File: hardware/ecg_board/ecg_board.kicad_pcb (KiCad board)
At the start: 2 copper layers, 53 parts, among them J1 USB_C_Receptacle_USB2.0_16P, J3 MEM2075-00-140-01-A, Q1 PMOS, U1 ESP32-S3-WROOM-1, U2 TLV75801PDBV, U3 AD8232, U4 MCP73832-2-OT, U5 USBLC6-2P6

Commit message: updated schematic and finish pcb v1
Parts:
- added BT1: Battery_Cell, Battery:battery_pads, F.Cu at (107.2, 69.4)
- added SW1: SW_SPDT, Button_Switch_SMD:SW_SPDT_PCM12, F.Cu at (109.4, 60.7)
- C10, C12, C13, C14: footprint Capacitor_SMD:C_0603_1608Metric -> Capacitor_SMD:C_0805_2012Metric
- E1, E2, E3: moved to B.Cu
- moved U3 132.8 mm to (179.5, 70.3), turned to 90 degrees
- moved E1 114.9 mm to (157.3, 97.1), turned to 180 degrees
- moved U2 94.0 mm to (134.7, 79.0)
- moved J3 93.5 mm to (197.6, 96.4), turned to 90 degrees
- moved U1 89.7 mm to (138.2, 101.5), turned to 180 degrees
- moved U5 89.4 mm to (149.9, 74.5), turned to 180 degrees
- moved U4 89.0 mm to (129.9, 65.0), turned to -90 degrees
- moved C9 82.2 mm to (148.9, 106.2), turned to -90 degrees
- moved C4 81.4 mm to (186.7, 68.8), turned to -90 degrees
- moved D1 81.4 mm to (133.1, 74.9), turned to -90 degrees
- moved C10 80.8 mm to (150.7, 106.4), turned to -90 degrees
- moved C5 78.9 mm to (183.7, 72.2), turned to 90 degrees
- moved C1 78.5 mm to (176.4, 74.8), turned to 180 degrees
- moved C6 76.9 mm to (181.4, 74.8)
- moved R13 76.8 mm to (189.7, 72.2), turned to -90 degrees
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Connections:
- net +BATT renamed Net-(Q1-D)
- net /RL renamed /LL
- C12 pad 2: +5V -> VDD
- J1 pad A6: unconnected-(J1-D+-PadA6) -> Net-(J1-D+-PadA6)
- J1 pad B5: Net-(J1-CC1) -> Net-(J1-CC2)
- J1 pad B6: unconnected-(J1-D+-PadB6) -> Net-(J1-D+-PadA6)
- J1 pad B7: unconnected-(J1-D--PadB7) -> Net-(J1-D--PadA7)
- R1 pad 1: unconnected-(R1-Pad1) -> Net-(J1-CC2)
- R2 pad 1: unconnected-(R2-Pad1) -> Net-(J1-CC1)
- U1 pad 26: /CS_SD -> unconnected-(U1-IO45-Pad26)
- U1 pad 33: /SCK -> unconnected-(U1-IO40-Pad33)
- U1 pad 34: /MISO -> unconnected-(U1-IO41-Pad34)
- U1 pad 35: /MOSI -> unconnected-(U1-IO42-Pad35)
- U1 pad 6: unconnected-(U1-IO6-Pad6) -> /MISO
- U1 pad 7: unconnected-(U1-IO7-Pad7) -> /SCK
- U1 pad 8: unconnected-(U1-IO15-Pad8) -> /MOSI
- U1 pad 9: unconnected-(U1-IO16-Pad9) -> /CS_SD
- U2 pad 1: +5V -> VDD
- U2 pad 3: +5V -> VDD
- U5 pad 3: Net-(J1-CC1) -> Net-(J1-D--PadA7)
- U5 pad 4: Net-(J1-D--PadA7) -> Net-(J1-D+-PadA6)
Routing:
- net +3V3: track 0.00 -> 93.8 mm, vias 0 -> 4
- net /RA: track 0.00 -> 84.7 mm, vias 0 -> 1
- net /SIG_OUT: track 0.00 -> 78.6 mm, vias 0 -> 2
- net /LO+: track 0.00 -> 54.2 mm, vias 0 -> 2
- net /LO-: track 0.00 -> 52.4 mm, vias 0 -> 2
- net +5V: track 0.00 -> 49.9 mm, vias 0 -> 3
- net Net-(Q1-D): track 0.00 -> 44.9 mm, vias 0 -> 2
- net /MOSI: track 0.00 -> 39.5 mm
- net /CS_SD: track 0.00 -> 39.5 mm
- net /SCK: track 0.00 -> 39.1 mm
- net /MISO: track 0.00 -> 38.8 mm
- net Net-(U3-SW): track 0.00 -> 28.7 mm, vias 0 -> 2
- net Net-(U3-IAOUT): track 0.00 -> 28.5 mm, vias 0 -> 2
- net /REFOUT: track 0.00 -> 28.3 mm, vias 0 -> 2
- net Net-(R17-Pad2): track 0.00 -> 21.8 mm, vias 0 -> 2
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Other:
- board outline added: 112 x 55.9 mm
- copper layers 2 -> 4
- board text added: "BATTERY"
- board text added: "FINGER ECG"

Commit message: added components and created bom
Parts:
- added C16: 220nF, Capacitor_SMD:C_0603_1608Metric, F.Cu at (176.4, 76.5)
- added C17: 220nF, Capacitor_SMD:C_0603_1608Metric, F.Cu at (165.8, 66.8)
- added R23: 470k, Resistor_SMD:R_0603_1608Metric, F.Cu at (168.3, 69.3)
- added R25: 220k, Resistor_SMD:R_0603_1608Metric, F.Cu at (183.8, 80.9)
- C1, C7: value 0.33uF -> 100nF
- C14: footprint Capacitor_SMD:C_0805_2012Metric -> Capacitor_SMD:C_0603_1608Metric
- C4: value 1.5nF -> 1nF
- D3: moved to B.Cu
- J1: footprint Connector_USB:USB_C_Receptacle_GCT_USB4105-xx-A_16P_TopMnt_Horizontal -> Connector_USB:USB_C_Receptacle_HCTL_HC-TYPE-C-16P-01A
- Q1: value PMOS -> NX3008PBK,215
- R14: value 360k -> 220k
- R15, R16: value 180k -> 220k
- R5: value 1.4M -> 1M
- moved C11 1.73 mm to (150.2, 102.3)
- moved R19 1.68 mm to (166.0, 70.2)
- moved R22 1.55 mm to (150.2, 103.9)
- moved D3 1.28 mm to (137.5, 67.2), turned to 180 degrees
- moved R1 0.98 mm to (147.5, 71.9)
- moved R2 0.90 mm to (152.1, 71.8)
- moved R15 0.75 mm to (179.8, 79.1)
- moved R16 0.75 mm to (177.7, 79.1)
- moved R17 0.75 mm to (175.7, 79.1)
- moved R18 0.75 mm to (181.7, 79.1)
- moved R14 0.58 mm to (183.8, 77.8)
- moved C7 0.20 mm to (167.5, 66.8)
- moved SW1 0.16 mm to (109.4, 60.8)
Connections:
- R14 pad 1: /LL -> Net-(R14-Pad1)
- R5 pad 2: Net-(U3-SW) -> Net-(R23-Pad1)
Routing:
- net +3V3: track 93.8 -> 167.3 mm, vias 4 -> 5
- net GND: track 0.00 -> 17.8 mm, vias 0 -> 45
- net /LA: track 17.7 -> 28.6 mm
- net /LL: track 7.26 -> 15.5 mm
- net Net-(R17-Pad2): track 21.8 -> 27.5 mm
- net /D-: track 14.0 -> 19.5 mm
- net /D+: track 14.3 -> 18.6 mm
- net Net-(J1-D--PadA7): track 7.68 -> 10.8 mm
- net Net-(J1-D+-PadA6): track 7.68 -> 10.6 mm
- net /REFOUT: track 28.3 -> 30.7 mm
- net VDD: track 10.9 -> 13.3 mm
- net Net-(D3-A): track 1.67 -> 3.46 mm, vias 0 -> 1
- net Net-(C4-Pad2): track 3.00 -> 4.73 mm
- net Net-(U3-HPSENSE): track 6.19 -> 7.86 mm
- net Net-(U3-HPDRIVE): track 3.21 -> 4.88 mm
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- added copper zone on B.Cu, net GND
- added copper zone on F.Cu, net GND
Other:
- outline, holes or cut-outs redrawn
- copper layers 4 -> 2
- board text removed: "FINGER ECG"

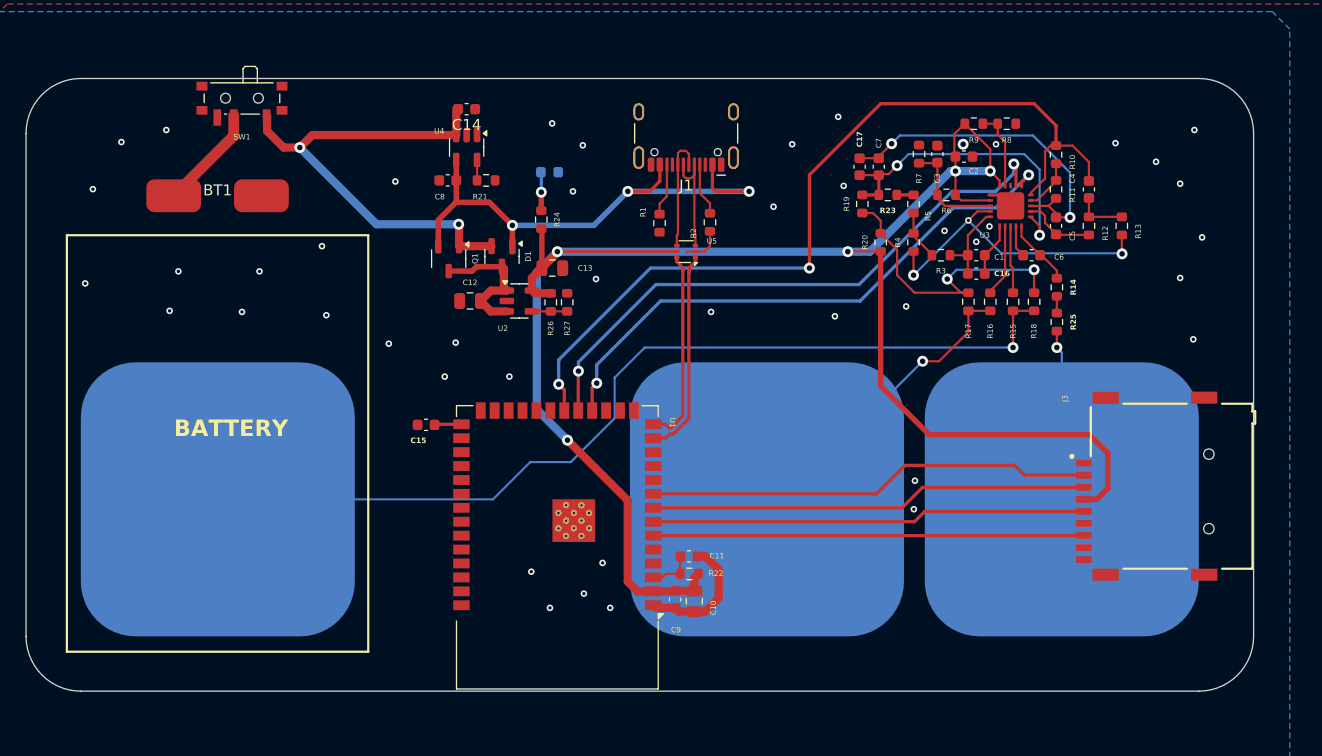
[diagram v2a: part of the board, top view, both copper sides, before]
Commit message: moved switch and fixed bom
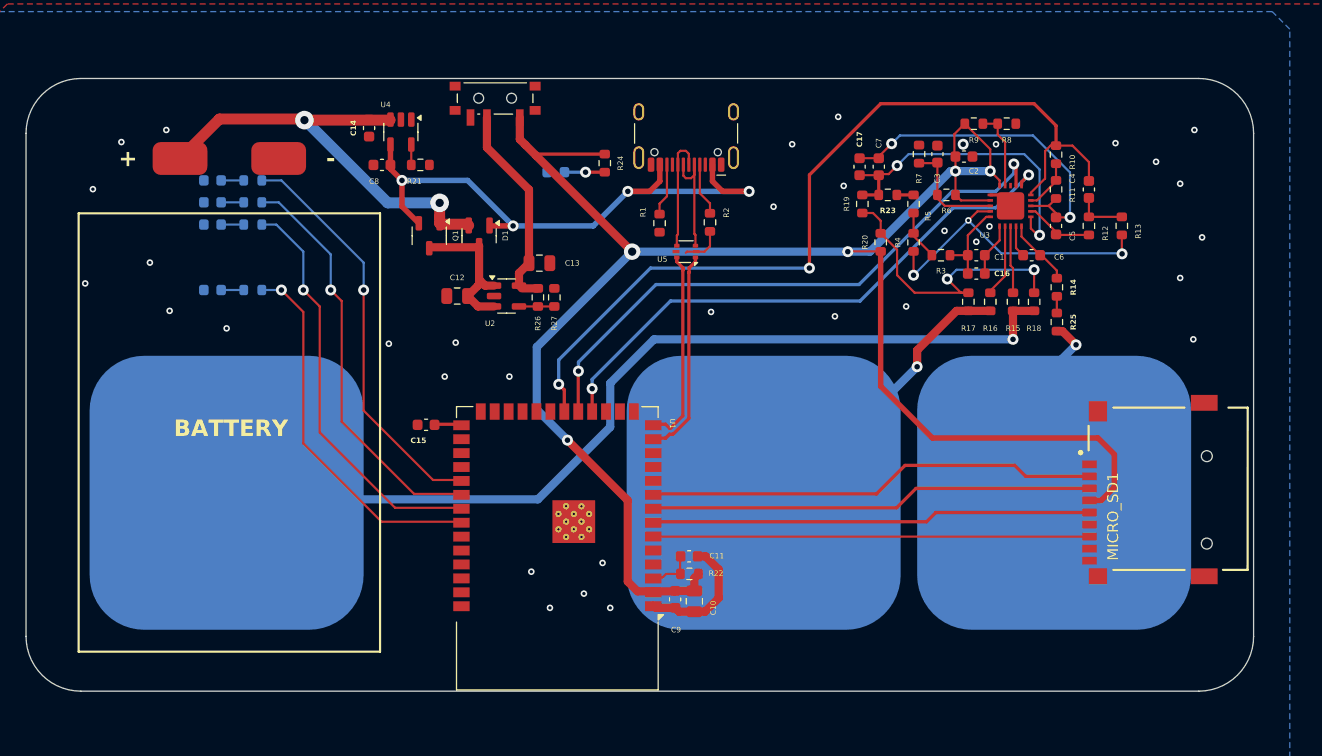
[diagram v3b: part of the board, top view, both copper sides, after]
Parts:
- removed J3: MEM2075-00-140-01-A, MEM2075_00_140_01_A:GCT_MEM2075-00-140-01-A
- added D2: LED, LED_SMD:LED_0603_1608Metric, B.Cu at (106.7, 72.0)
- added D4: LED, LED_SMD:LED_0603_1608Metric, B.Cu at (106.7, 70.0)
- added D5: LED, LED_SMD:LED_0603_1608Metric, B.Cu at (106.7, 68.0)
- added D6: LED, LED_SMD:LED_0603_1608Metric, B.Cu at (106.7, 78.0)
- added MICRO_SD1: TF-01A, TF-01A:TF-01A, F.Cu at (193.9, 96.1)
- added R28: 2k, Resistor_SMD:R_0603_1608Metric, B.Cu at (110.4, 72.0)
- added R29: 2k, Resistor_SMD:R_0603_1608Metric, B.Cu at (110.4, 70.0)
- added R30: 2k, Resistor_SMD:R_0603_1608Metric, B.Cu at (110.4, 68.0)
- added R31: 2k, Resistor_SMD:R_0603_1608Metric, B.Cu at (110.4, 78.0)
- moved SW1 23.1 mm to (132.5, 60.8)
- moved C14 9.07 mm to (121.0, 63.2), turned to 90 degrees
- moved R24 7.75 mm to (142.5, 66.4)
- moved C8 6.16 mm to (122.2, 66.6)
- moved R21 6.16 mm to (125.7, 66.6)
- moved U4 6.16 mm to (123.9, 63.6)
- moved BT1 3.57 mm to (108.2, 66.0)
- moved D1 2.81 mm to (131.0, 73.0)
- moved Q1 2.74 mm to (126.5, 73.0)
- moved C12 1.26 mm to (129.0, 78.5)
- moved C13 1.26 mm to (136.5, 75.5)
- moved U2 1.26 mm to (133.5, 78.5)
- moved R26 1.26 mm to (136.4, 78.7)
- moved R27 1.26 mm to (137.9, 78.7)
- moved E2 1.00 mm to (108.0, 96.5)
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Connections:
- C13 pad 2: +3V3 -> Net-(SW1-B)
- C14 pad 2: Net-(Q1-D) -> +BATT
- D1 pad 2: Net-(Q1-D) -> +BATT
- Q1 pad 1: Net-(Q1-D) -> +BATT
- R24 pad 1: Net-(D3-A) -> +3V3
- R24 pad 2: +3V3 -> Net-(D3-A)
- R26 pad 1: +3V3 -> Net-(SW1-B)
- SW1 pad 1: Net-(Q1-D) -> +3V3
- SW1 pad 2: +BATT -> Net-(SW1-B)
- U1 pad 31: unconnected-(U1-IO38-Pad31) -> /RECORDING
- U1 pad 32: unconnected-(U1-IO39-Pad32) -> /LEADS_ON
- U1 pad 33: unconnected-(U1-IO40-Pad33) -> /LEADS_OFF
- U1 pad 34: unconnected-(U1-IO41-Pad34) -> /EXTRA
- U2 pad 5: +3V3 -> Net-(SW1-B)
- U4 pad 3: Net-(Q1-D) -> +BATT
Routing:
- net Net-(Q1-D): track 44.9 -> 0.00 mm, vias 2 -> 0
- net /LEADS_OFF: track 0.00 -> 37.7 mm, vias 0 -> 1
- net /LEADS_ON: track 0.00 -> 37.6 mm, vias 0 -> 1
- net /RECORDING: track 0.00 -> 37.3 mm, vias 0 -> 1
- net /EXTRA: track 0.00 -> 34.0 mm, vias 0 -> 1
- net +BATT: track 9.56 -> 40.7 mm, vias 0 -> 2
- net Net-(SW1-B): track 0.00 -> 19.1 mm
- net +5V: track 49.9 -> 55.3 mm, vias 3 -> 4
- net Net-(D6-A): track 0.00 -> 2.06 mm
- net Net-(D5-A): track 0.00 -> 2.06 mm
- net Net-(D4-A): track 0.00 -> 2.06 mm
- net Net-(D2-A): track 0.00 -> 2.06 mm
- net /RA: track 85.8 -> 87.5 mm
- net /LL: track 15.5 -> 16.9 mm
- net /MISO: track 38.8 -> 39.8 mm
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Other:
- board text added: "+"
- board text added: "-"
- board text added: "STATUS"

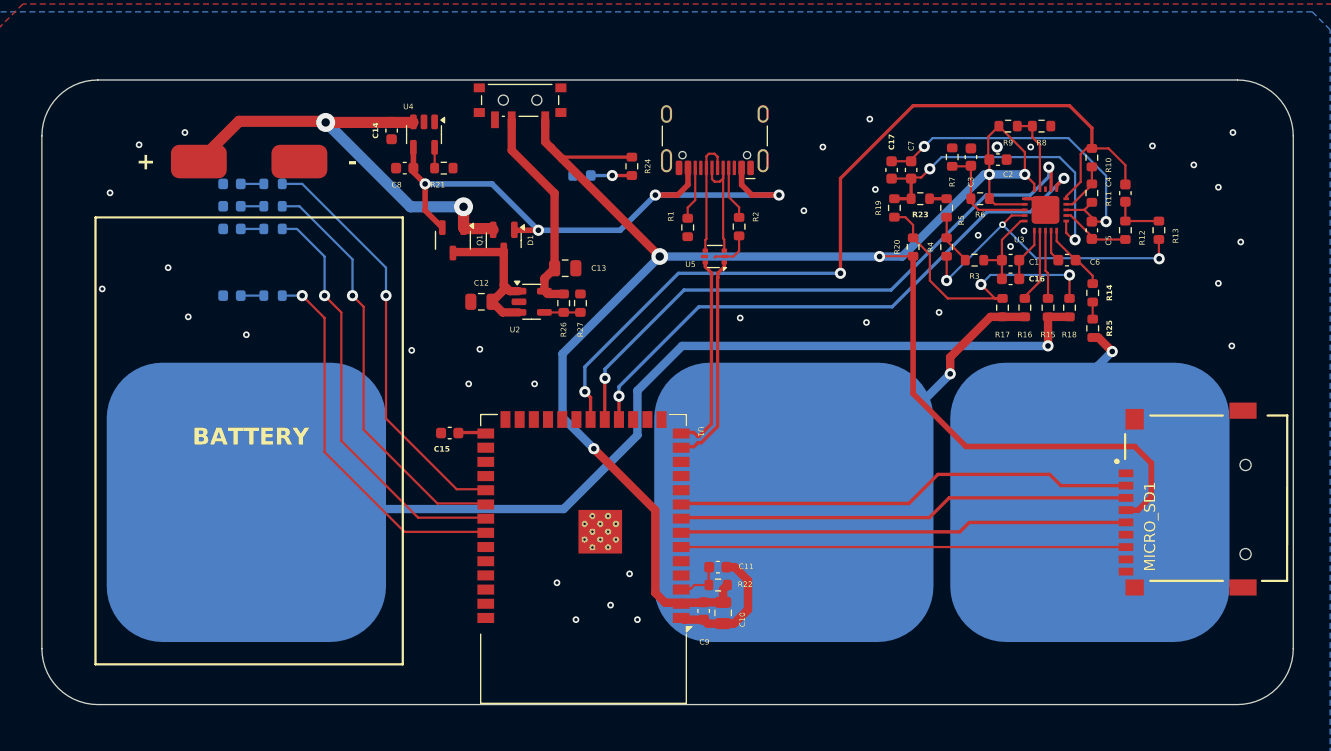
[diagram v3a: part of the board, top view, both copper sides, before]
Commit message: added debugging pads
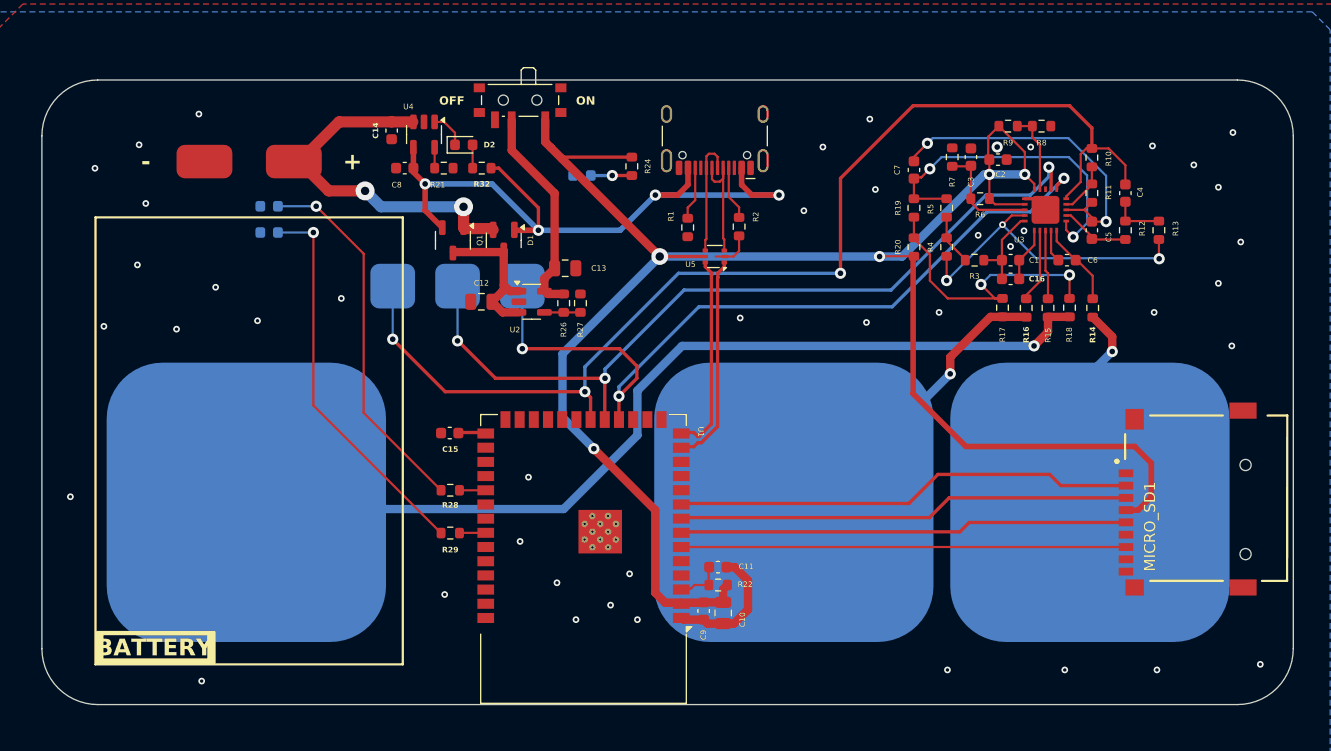
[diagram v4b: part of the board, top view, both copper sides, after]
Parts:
- removed C17: 220nF, Capacitor_SMD:C_0603_1608Metric
- removed D6: LED, LED_SMD:LED_0603_1608Metric
- removed R23: 470k, Resistor_SMD:R_0603_1608Metric
- removed R25: 220k, Resistor_SMD:R_0603_1608Metric
- removed R30, R31: 2k, Resistor_SMD:R_0603_1608Metric
- added LO+: ~, DebugPad:DebugPad, B.Cu at (126.9, 77.2)
- added LO-: ~, DebugPad:DebugPad, B.Cu at (132.7, 77.2)
- added R32: 2k, Resistor_SMD:R_0603_1608Metric, F.Cu at (129.1, 66.6)
- added SIG: ~, DebugPad:DebugPad, B.Cu at (121.1, 77.2)
- C1, C7: value 100nF -> .33uF
- C4: value 1nF -> 1.5nF
- D2, R28, R29: moved to F.Cu
- R14: value 220k -> 360k
- R15, R16: value 220k -> 180k
- R5: value 1M -> 1.4M
- moved R29 33.3 mm to (126.2, 99.2)
- moved R28 28.3 mm to (126.2, 95.4)
- moved D2 22.1 mm to (127.5, 64.5)
- moved D5 5.48 mm to (110.0, 72.3)
- moved D4 3.32 mm to (110.0, 70.0)
- moved R19 1.75 mm to (167.8, 70.2)
- moved R14 1.35 mm to (183.8, 79.1)
- moved C7 0.25 mm to (167.8, 66.8)
- moved R16 0.13 mm to (177.8, 79.1)
- moved R20 0.07 mm to (167.8, 73.7)
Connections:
- D2 pad 1: GND -> /CHG_STAT
- R14 pad 1: Net-(R14-Pad1) -> /LL
- R28 pad 1: Net-(D2-A) -> Net-(D4-A)
- R28 pad 2: /LEADS_OFF -> /LEADS_ON
- R29 pad 1: Net-(D4-A) -> Net-(D5-A)
- R29 pad 2: /LEADS_ON -> /EXTRA
- R5 pad 2: Net-(R23-Pad1) -> Net-(U3-SW)
- U1 pad 31: /RECORDING -> /LEADS_ON
- U1 pad 32: /LEADS_ON -> unconnected-(U1-IO39-Pad32)
- U1 pad 33: /LEADS_OFF -> unconnected-(U1-IO40-Pad33)
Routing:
- net /LEADS_OFF: track 37.7 -> 0.00 mm, vias 1 -> 0
- net /RECORDING: track 37.3 -> 0.00 mm, vias 1 -> 0
- net /LEADS_ON: track 37.6 -> 2.35 mm, vias 1 -> 0
- net Net-(D5-A): track 2.06 -> 34.8 mm, vias 0 -> 1
- net /EXTRA: track 34.0 -> 2.36 mm, vias 1 -> 0
- net Net-(D4-A): track 2.06 -> 33.5 mm, vias 0 -> 1
- net /SIG_OUT: track 78.6 -> 102.5 mm, vias 2 -> 3
- net /LO-: track 51.6 -> 71.5 mm, vias 2 -> 3
- net /LO+: track 54.2 -> 73.7 mm, vias 2 -> 3
- net +BATT: track 40.7 -> 32.6 mm
- net +5V: track 55.3 -> 63.0 mm
- net +3V3: track 167.6 -> 171.6 mm
- net /CHG_STAT: track 0.00 -> 3.30 mm
- net /RA: track 87.5 -> 84.7 mm
- net Net-(D6-A): track 2.06 -> 0.00 mm
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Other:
- board text added: "IO41"
- board text added: "LEADS ON"
- board text added: "OFF"
- board text added: "ON"
- board text added: "PWR"
- board text removed: "STATUS"
